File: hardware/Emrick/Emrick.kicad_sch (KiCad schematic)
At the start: 88 parts, among them J1 LED_STRIP_CONNECTOR, J2 UFL, J3 Conn_02x05_Odd_Even, J4 BATT_CONN, P1 USB_C_Plug_USB2.0, Q1 Q_NMOS_GSD, Q2 Q_NMOS_GSD, Q3 Q_NMOS_GSD, SW1 SW_SPST, U1 74HCT541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

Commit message: add revision 3 gerber files
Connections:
- net BAT_PGOOD: now also U2.40 (DIO_27); no longer U2.42 (DIO_29)
- net HALF_VBAT: now also U2.42 (DIO_29); no longer U2.32 (DIO_22)
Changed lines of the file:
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@@
   (no_connect (at 44.45 267.97))
   (no_connect (at 45.72 172.72))
+  (no_connect (at 217.17 91.44))
   (no_connect (at 217.17 106.68))
-  (no_connect (at 217.17 104.14))
   (no_connect (at 217.17 101.6))
   (no_connect (at 217.17 93.98))
@@
     )
   )
-  (global_label "HALF_VBAT" (shape input) (at 217.17 91.44 0) (fields_autoplaced)
-    (effects (font (size 1.27 1.27)) (justify left))
-    (property "Intersheetrefs" "${INTERSHEET_REFS}" (at 229.994 91.44 0)
+  (global_label "HALF_VBAT" (shape input) (at 217.17 109.22 0) (fields_autoplaced)
+    (effects (font (size 1.27 1.27)) (justify left))
+    (property "Intersheetrefs" "${INTERSHEET_REFS}" (at 229.994 109.22 0)
       (effects (font (size 1.27 1.27)) (justify left) hide)
     )
@@
     )
   )
-  (global_label "BAT_PGOOD" (shape input) (at 217.17 109.22 0) (fields_autoplaced)
-    (effects (font (size 1.27 1.27)) (justify left))
-    (property "Intersheetrefs" "${INTERSHEET_REFS}" (at 230.3479 109.1406 0)
-      (effects (font (size 1.27 1.27)) (justify left) hide)
-    )
+  (global_label "BAT_PGOOD" (shape input) (at 217.17 104.14 0) (fields_autoplaced)
+    (effects (font (size 1.27 1.27)) (justify left))
+    (property "Intersheetrefs" "${INTERSHEET_REFS}" (at 230.3479 104.0606 0)
+      (effects (font (size 1.27 1.27)) (justify left) hide)
+    )

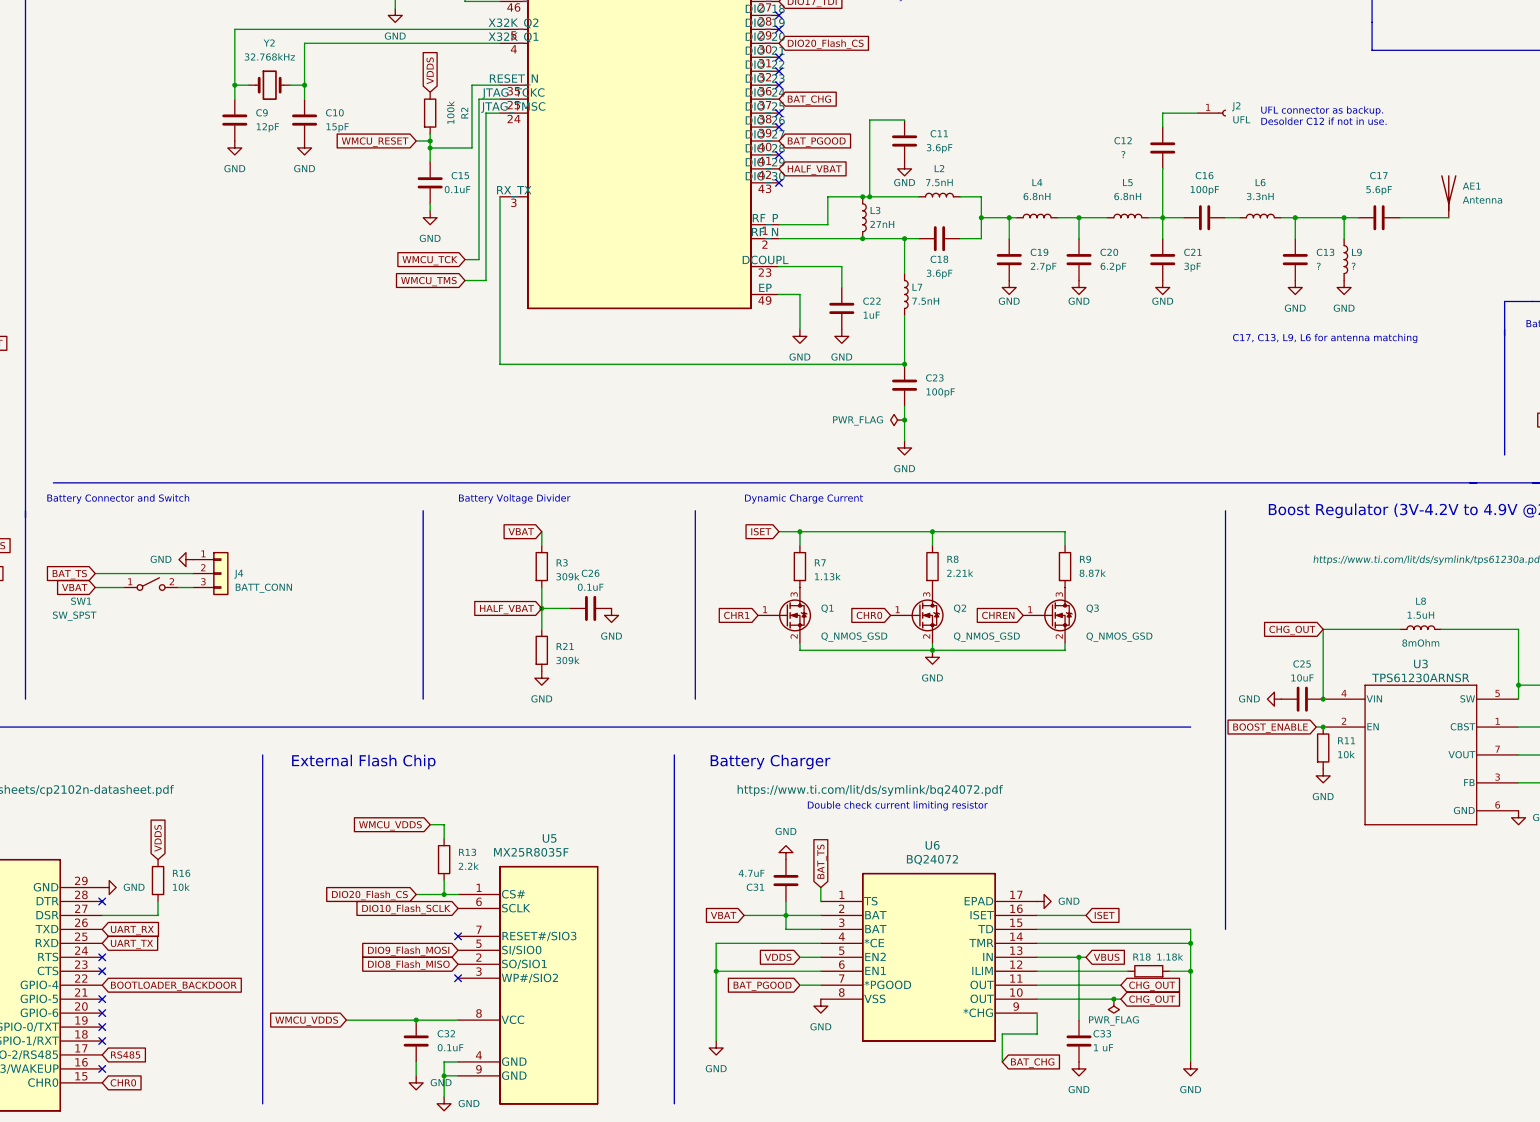
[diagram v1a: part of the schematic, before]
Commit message: Update schematic and pcb to revision 4
- Add a new switch footprint
- Add a line to reset the CC1310 from the CP2102x
- Switch to a 433MHz - 510MHz antenna
- Decrease the dimensions of the board
- Add a wireframe of the battery dimensions
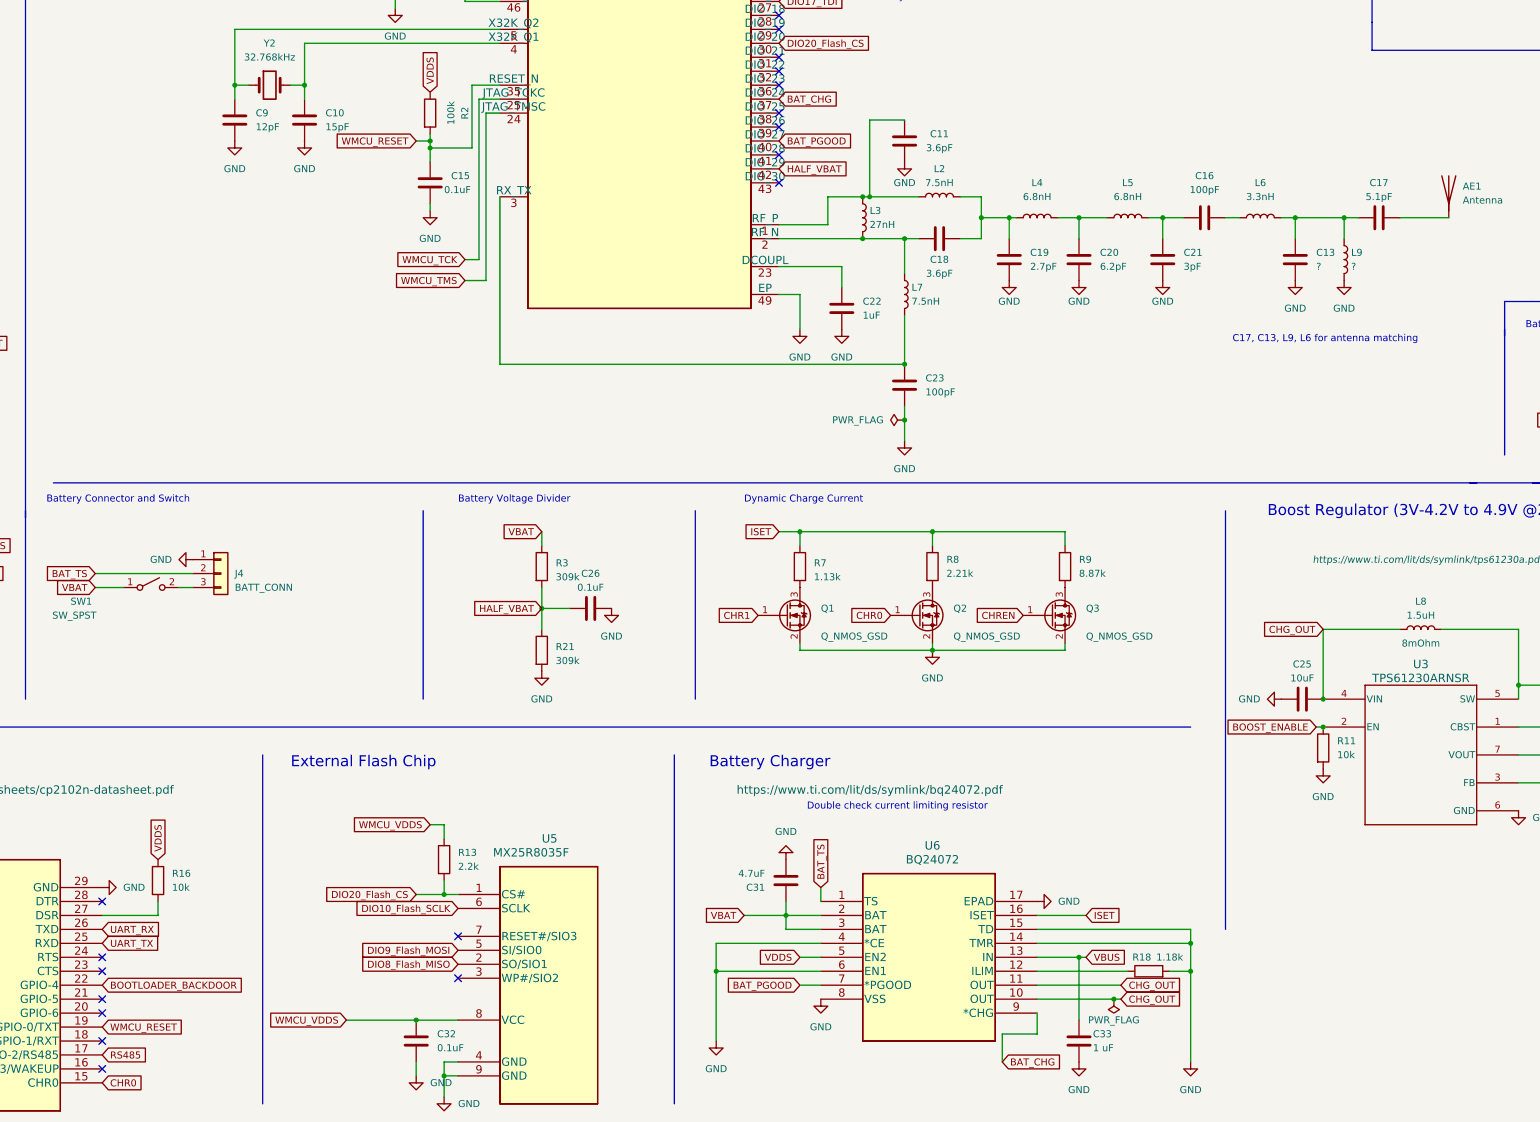
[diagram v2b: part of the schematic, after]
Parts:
- removed C12: ?, Capacitor_SMD:C_0402_1005Metric, symbol Device:C
- removed J2: UFL, Connector_Coaxial:U.FL_Hirose_U.FL-R-SMT-1_Vertical, symbol Connector:Conn_01x01_Female
- AE1: footprint Emrick Footprints:emrick_custom_antenna -> RF_Antenna:Texas_SWRA416_868MHz_915MHz
- C17: value 5.6pF -> 5.1pF
- SW1: footprint xkbswitch:SS-12D10G5_XKB -> xkbconnectivity:SW-TH_SS-12D11G4R
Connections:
- net WMCU_RESET: now also U4.19 (GPIO-0/TXT)
- no-connect marks 35 -> 34
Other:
- note removed: "UFL connector as backup. Desolder C12 if not in use."
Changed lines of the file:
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@@
     (title "Project Emrick Light Strip")
     (date "2022-10-10")
-    (rev "3")
+    (rev "4")
   )
   (junction (at 36.83 43.18) (diameter 0) (color 0 0 0 0)
@@
   (no_connect (at 93.98 267.97))
   (no_connect (at 93.98 273.05))
-  (no_connect (at 93.98 265.43))
   (no_connect (at 93.98 262.89))
   (no_connect (at 93.98 252.73))
@@
     (stroke (width 0) (type default))
   )
-  (wire (pts (xy 287.02 101.6) (xy 287.02 99.06))
-    (stroke (width 0) (type default))
-  )
   (wire (pts (xy 160.02 78.74) (xy 166.37 78.74))
     (stroke (width 0) (type default))
@@
     (stroke (width 0) (type default))
   )
-  (wire (pts (xy 287.02 109.22) (xy 287.02 118.11))
-    (stroke (width 0) (type default))
-  )
   (wire (pts (xy 269.24 196.85) (xy 245.11 196.85))
     (stroke (width 0) (type default))
@@
     (stroke (width 0) (type default))
   )
-  (wire (pts (xy 287.02 99.06) (xy 293.37 99.06))
-    (stroke (width 0) (type default))
-  )
   (wire (pts (xy 160.02 125.73) (xy 162.56 125.73))
     (stroke (width 0) (type default))
@@
     (effects (font (size 1.27 1.27)) (justify left bottom))
   )
-  (text "UFL connector as backup. \nDesolder C12 if not in use. "
-    (at 304.8 101.6 0)
-    (effects (font (size 1.27 1.27)) (justify left bottom))
-  )
   (text "Boost Regulator (3V-4.2V to 4.9V @2A)\n" (at 306.07 172.72 0)
     (effects (font (size 2 2)) (justify left bottom))
@@
     )
   )
+  (global_label "WMCU_RESET" (shape input) (at 93.98 265.43 0) (fields_autoplaced)
+    (effects (font (size 1.27 1.27)) (justify left))
+    (property "Intersheetrefs" "${INTERSHEET_REFS}" (at 109.1018 265.43 0)
+      (effects (font (size 1.27 1.27)) (justify left) hide)
+    )
+  )
   (global_label "VDDS" (shape input) (at 125.73 31.75 90) (fields_autoplaced)
     (effects (font (size 1.27 1.27)) (justify left))
@@
       (effects (font (size 1.27 1.27)))
     )
-    (property "Footprint" "xkbswitch:SS-12D10G5_XKB" (at 102.87 185.42 0)
+    (property "Footprint" "xkbconnectivity:SW-TH_SS-12D11G4R" (at 102.87 185.42 0)
       (effects (font (size 1.27 1.27)) hide)
     )
@@
     )
   )
-  (symbol (lib_id "Device:C") (at 287.02 105.41 0) (unit 1)
-    (in_bom yes) (on_board yes) (dnp no)
-    (property "Reference" "C12" (at 278.13 104.14 0)
-      (effects (font (size 1.27 1.27)) (justify left))
-    )
-    (property "Value" "?" (at 279.4 106.68 0)
-      (effects (font (size 1.27 1.27)) (justify left))
-    )
-    (property "Footprint" "Capacitor_SMD:C_0402_1005Metric" (at 287.9852 109.22 0)
-      (effects (font (size 1.27 1.27)) hide)
-    )
-    (property "Datasheet" "~" (at 287.02 105.41 0)
-      (effects (font (size 1.27 1.27)) hide)
-    )
-    (pin "1")
-    (pin "2")
-    (instances
-      (project "Emrick"
-        (path "/3273eadb-35bb-41d4-911c-7b885ba92916"
-          (reference "C12") (unit 1)
-        )
-      )
-    )
-  )
   (symbol (lib_id "power:GND") (at 62.23 170.18 90) (unit 1)
     (in_bom yes) (on_board yes) (dnp no) (fields_autoplaced)
@@
       (effects (font (size 1.27 1.27)) (justify left))
     )
-    (property "Footprint" "Emrick Footprints:emrick_custom_antenna" (at 339.09 113.03 0)
+    (property "Footprint" "RF_Antenna:Texas_SWRA416_868MHz_915MHz" (at 339.09 113.03 0)
       (effects (font (size 1.27 1.27)) hide)
     )
@@
   (symbol (lib_id "Device:C") (at 326.39 118.11 90) (unit 1)
     (in_bom yes) (on_board yes) (dnp no) (fields_autoplaced)
-    (property "Reference" "C17" (at 326.39 110.49 90)
+    (property "Reference" "C17" (at 326.39 111.76 90)
       (effects (font (size 1.27 1.27)))
     )
-    (property "Value" "5.6pF" (at 326.39 113.03 90)
+    (property "Value" "5.1pF" (at 326.39 114.3 90)
       (effects (font (size 1.27 1.27)))
     )
@@
         )
       )
-    )
-  )
-  (symbol (lib_id "Connector:Conn_01x01_Female") (at 298.45 99.06 0) (unit 1)
-    (in_bom yes) (on_board yes) (dnp no) (fields_autoplaced)
-    (property "Reference" "J2" (at 299.72 97.7899 0)
-      (effects (font (size 1.27 1.27)) (justify left))
-    )
-    (property "Value" "UFL" (at 299.72 100.3299 0)
-      (effects (font (size 1.27 1.27)) (justify left))
-    )
-    (property "Footprint" "Connector_Coaxial:U.FL_Hirose_U.FL-R-SMT-1_Vertical" (at 298.45 99.06 0)
-      (effects (font (size 1.27 1.27)) hide)
-    )
-    (property "Datasheet" "~" (at 298.45 99.06 0)
-      (effects (font (size 1.27 1.27)) hide)
-    )
-    (pin "1")
-    (instances
-      (project "Emrick"
-        (path "/3273eadb-35bb-41d4-911c-7b885ba92916"
-          (reference "J2") (unit 1)
-        )
-      )

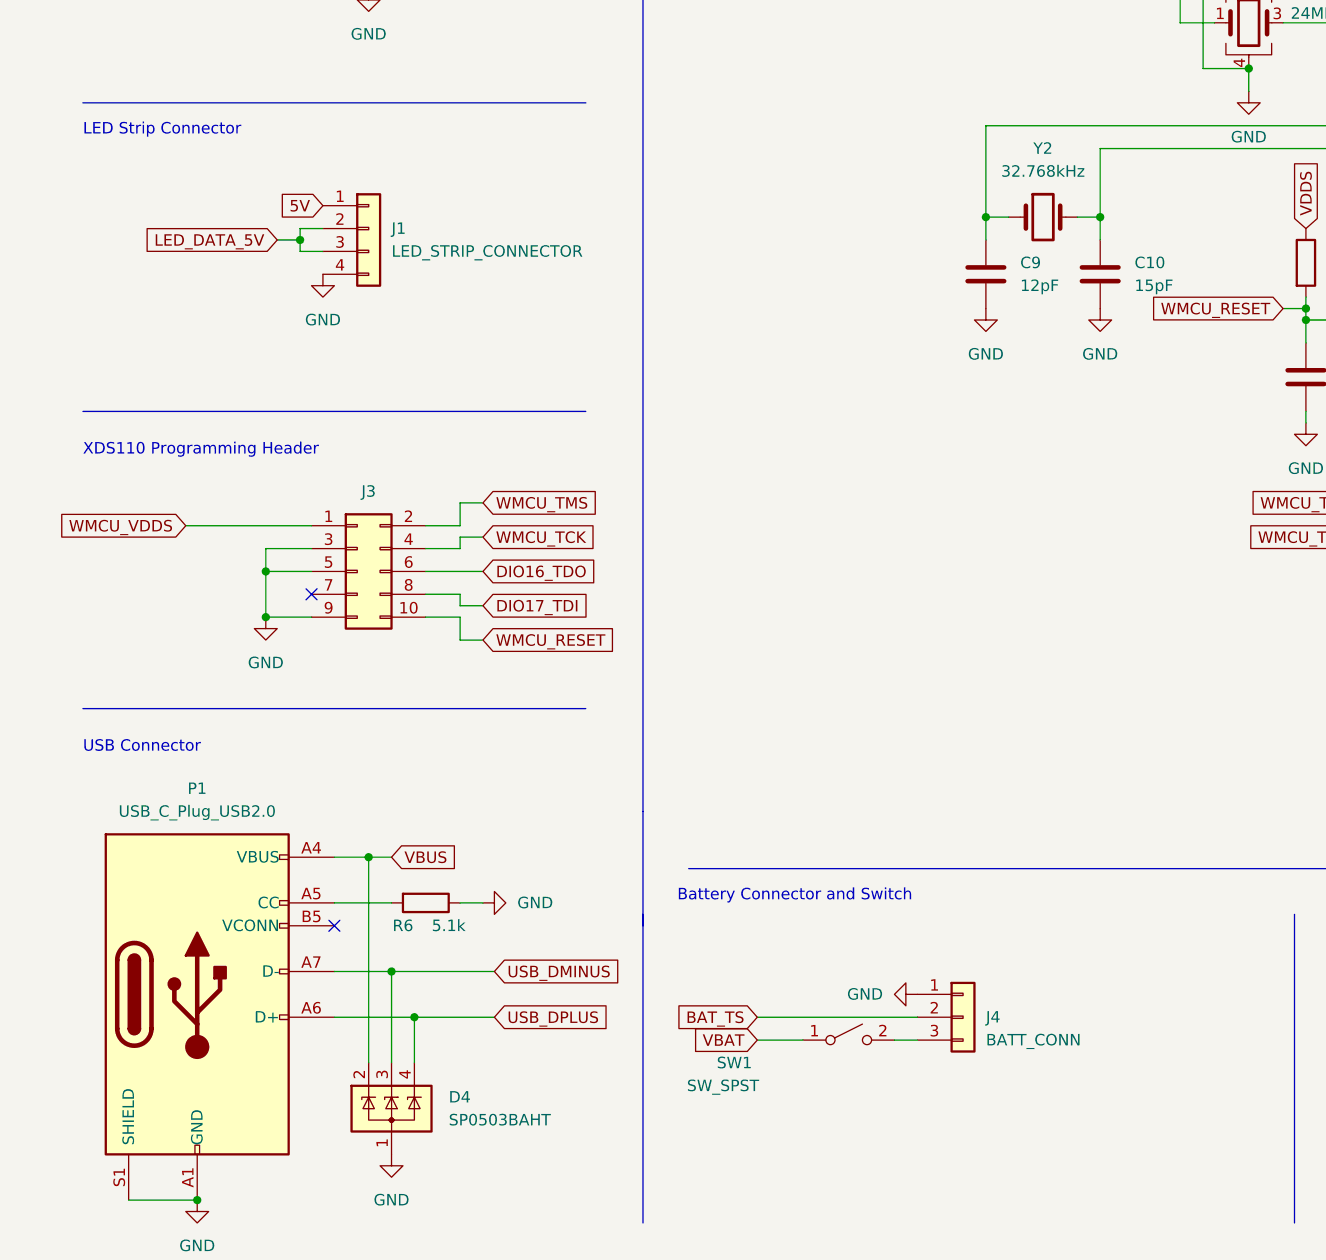
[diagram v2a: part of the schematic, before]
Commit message: Finalize revision 4
- Added rev4 bom
- Updated production files in hardware\Emrick\production
- Fixed/ignored all errors in board PCB
- Added AAMB graphics
- Changed connector to JST PA 4 pin for mechanical latch
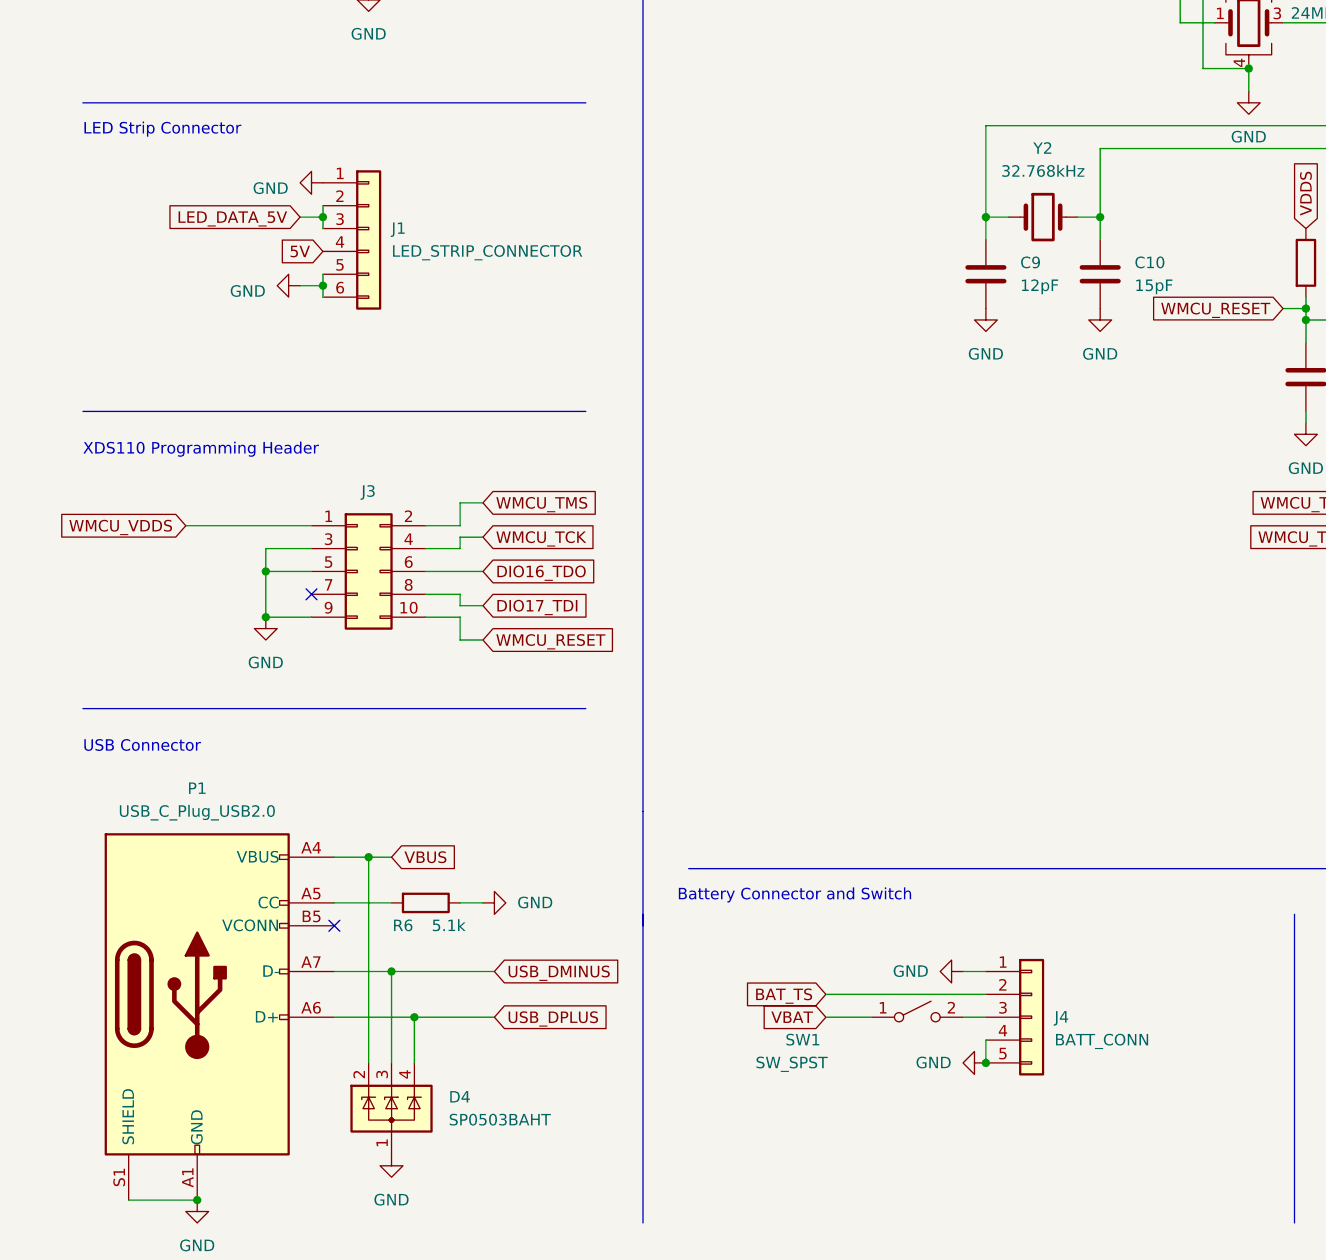
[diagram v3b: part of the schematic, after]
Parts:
- J1: footprint s4bjstconn:CONN_S4B-PH-SM4-TBLFSN_JST -> jstpa:CONN-SMD_BM04B-PASS-1-TFT; symbol Connector_Generic:Conn_01x04 -> Connector_Generic:Conn_01x06
- J4: symbol Connector_Generic:Conn_01x03 -> Connector_Generic:Conn_01x05
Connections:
- net 5V: now also J1.4 (Pin_4); no longer J1.1 (Pin_1)
- net GND: now also J1.1 (Pin_1), J1.5 (Pin_5), J1.6 (Pin_6), J4.4 (Pin_4), J4.5 (Pin_5); no longer J1.4 (Pin_4)
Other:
- moved on the sheet: SW1
